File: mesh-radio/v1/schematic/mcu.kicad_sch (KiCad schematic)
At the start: 34 parts, among them U8 NRF52840-QIAA-F-R7, Y1 32MHz, Y2 32.768kHz

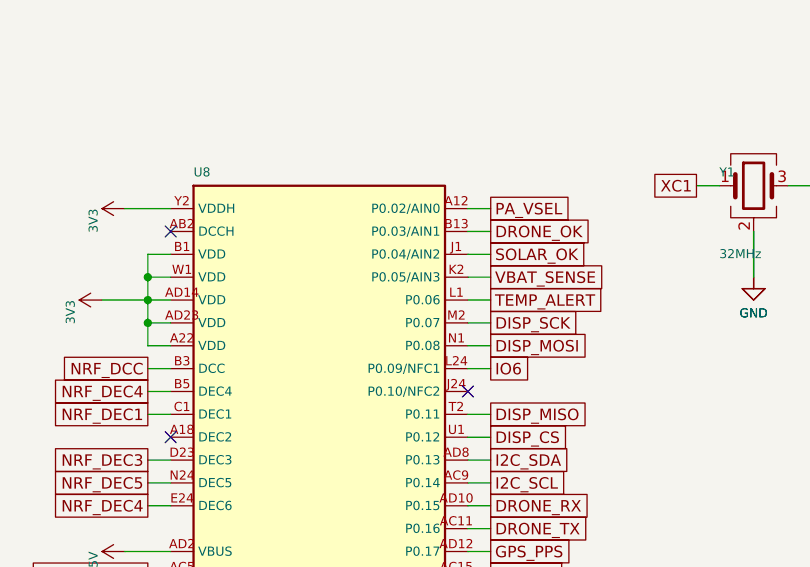
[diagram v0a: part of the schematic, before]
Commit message: Mesh Radio v1: fix every design-review finding, add the part audit
An independent review of the schematic found two critical and nine further
issues; all are fixed in src/circuit.py:
- reverse-battery FET gate now returns to the cell's own minus terminal, so
  a backwards cell stays isolated even while USB/solar/drone power the board
- solar and drone inputs: reverse-blocking Schottky + 22 V flat-clamp TVS
  (the 15 V TVS would have failed on a 12 V panel); 4.7 V clamp on every
  eFuse EN/UVLO pin so 20 V on an input stays inside its rating
- ideal diode (LM66100) holds VSYS on the cell when a 3 W burst trips the
  charger's 3.0 V battery disconnect
- charge LED moved to STAT2 (charging), USB cut-off lowered to 5.4 V,
  charger /CE on a GPIO for firmware temperature control, -40 C TCXO,
  power mux on only with the amplifier, header VSYS pin removed
- firmware ceilings documented: SX1262 +20 dBm, amplifier 3.6 V by default

docs/part-audit.md: all 125 lines checked at DigiKey and LCSC (genuine
LCSC numbers, DigiKey numbers, second sources for out-of-stock lines);
parts cost about $76 at 10 boards, $58 at 100.

Schematic regenerated: ERC 0 violations, netlist equals circuit.py.

Co-Authored-By: Claude Opus 5.5 <noreply@anthropic.com>
Claude-Session: https://claude.ai/code/session_015TBB2ThqxHSgA8MkFosmn9
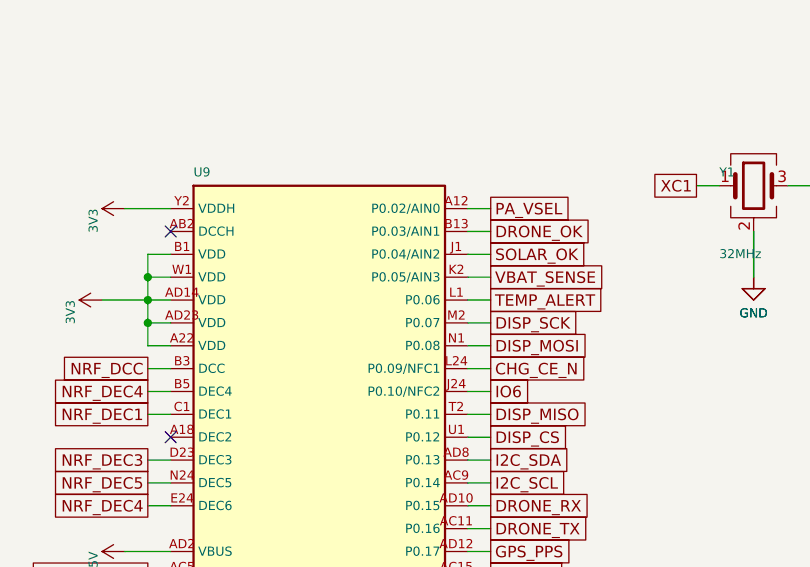
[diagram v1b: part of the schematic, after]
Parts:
- removed U8: NRF52840-QIAA-F-R7, og:AQFN-73_L7.0-W7.0-P0.50-BL-EP4.8, symbol og:NRF52840
- added U9: NRF52840-QIAA-F-R7, og:AQFN-73_L7.0-W7.0-P0.50-BL-EP4.8, symbol og:NRF52840
- AE1: DigiKey (none) -> 712-2450AT18A0100001ECT-ND
- C22, C27, C33, C34: DigiKey (none) -> 1276-1044-1-ND
- C23, C28: DigiKey (none) -> 1276-1067-1-ND
- C24, C25, C26, C30: DigiKey (none) -> 1276-1001-1-ND
- C29: DigiKey (none) -> 1276-1077-1-ND
- C31: DigiKey (none) -> 490-5922-1-ND
- C32: DigiKey (none) -> 490-3242-1-ND
- C35, C36: DigiKey (none) -> 1276-1178-1-ND
- C37, C38: DigiKey (none) -> 490-3113-1-ND
- C39: DigiKey (none) -> 490-6080-1-ND
- C40: DigiKey (none) -> 490-6077-1-ND
- C41: DigiKey (none) -> 490-6073-1-ND
- L2: DigiKey (none) -> 445-6396-1-ND
- L3: DigiKey (none) -> 490-1148-1-ND
- L4: DigiKey (none) -> 490-1139-1-ND
- L5: DigiKey (none) -> 490-6800-1-ND
- L6: DigiKey (none) -> 490-6813-1-ND
- R35, R36: DigiKey (none) -> 311-22.0LRCT-ND
- Y1: DigiKey (none) -> 535-13900-1-ND
- Y2: DigiKey (none) -> 535-9543-1-ND
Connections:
- net 3V3: now also U9.A22 (VDD), U9.AD14 (VDD), U9.AD23 (VDD), U9.B1 (VDD), U9.W1 (VDD), U9.Y2 (VDDH)
- net BTN_USER: now also U9.AD22 (P1.00)
- net CHG_STAT1: now also U9.AD20 (P0.24)
- net CHG_STAT2: now also U9.AC21 (P0.25)
- net DISP_BL: now also U9.P2 (P1.08)
- net DISP_CS: now also U9.U1 (P0.12)
- net DISP_DC: now also U9.G1 (P0.26)
- net DISP_MISO: now also U9.T2 (P0.11)
- net DISP_MOSI: now also U9.N1 (P0.08)
- net DISP_RST: now also U9.H2 (P0.27)
- net DISP_SCK: now also U9.M2 (P0.07)
- net DRONE_CTS: now also U9.AC17 (P0.21)
- net DRONE_OK: now also U9.B13 (P0.03/AIN1)
- net DRONE_RTS: now also U9.AD18 (P0.22)
- net DRONE_RX: now also U9.AD10 (P0.15)
- net DRONE_TX: now also U9.AC11 (P0.16)
- net GND: now also U9.0 (VSS (EP)), U9.B7 (VSS), U9.F23 (VSS_PA)
- net GPS_EN: now also U9.AC19 (P0.23)
- net GPS_PPS: now also U9.AD12 (P0.17)
- net GPS_RESET: now also U9.R1 (P1.09)
- net GPS_RX: now also U9.AC15 (P0.19)
- net GPS_TX: now also U9.AD16 (P0.20)
- net I2C_SCL: now also U9.AC9 (P0.14)
- net I2C_SDA: now also U9.AD8 (P0.13)
- net IO1: now also U9.B11 (P0.28/AIN4)
- net IO2: now also U9.A10 (P0.29/AIN5)
- net IO3: now also U9.B9 (P0.30/AIN6)
- net IO4: now also U9.A8 (P0.31/AIN7)
- net IO5: now also U9.W24 (P1.02)
- net IO6: now also U9.J24 (P0.10/NFC2)
- net LED_BLUE: now also U9.U24 (P1.04)
- net LED_GREEN: now also U9.V23 (P1.03)
- net LNA_EN: now also U9.T23 (P1.05)
- net LORA_BUSY: now also U9.B15 (P1.14)
- net LORA_DIO1: now also U9.A14 (P1.15)
- net LORA_MISO: now also U9.A16 (P1.13)
- net LORA_MOSI: now also U9.B17 (P1.12)
- net LORA_NRESET: now also U9.R24 (P1.06)
- net LORA_NSS: now also U9.A20 (P1.10)
- net LORA_SCK: now also U9.B19 (P1.11)
- net NRF_ANT: now also U9.H23 (ANT)
- net NRF_DCC: now also U9.B3 (DCC)
- net NRF_DEC1: now also U9.C1 (DEC1)
- net NRF_DEC3: now also U9.D23 (DEC3)
- net NRF_DEC4: now also U9.B5 (DEC4), U9.E24 (DEC6)
- net NRF_DEC5: now also U9.N24 (DEC5)
- net NRF_DECUSB: now also U9.AC5 (DECUSB)
- net NRF_DM: now also U9.AD4 (D-)
- net NRF_DP: now also U9.AD6 (D+)
- net NRF_RESET: now also U9.AC13 (P0.18/nRESET)
- net PA_EN: now also U9.P23 (P1.07)
- net PA_PWR_EN: now also U9.Y23 (P1.01)
- net PA_VSEL: now also U9.A12 (P0.02/AIN0)
- net SOLAR_OK: now also U9.J1 (P0.04/AIN2)
- net SWDCLK: now also U9.AA24 (SWDCLK)
- net SWDIO: now also U9.AC24 (SWDIO)
- net TEMP_ALERT: now also U9.L1 (P0.06)
- net USB_5V: now also U9.AD2 (VBUS)
- net VBAT_SENSE: now also U9.K2 (P0.05/AIN3)
- net XC1: now also U9.B24 (XC1)
- net XC2: now also U9.A23 (XC2)
- net XL1: now also U9.D2 (P0.00/XL1)
- net XL2: now also U9.F2 (P0.01/XL2)
- new net CHG_CE_N: U9.L24 (P0.09/NFC1)
- no-connect marks 4 -> 3

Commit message: Mesh radio v1: RF fixes from sim/rf (3 W heating, pad power, filter loss)
sim/rf found three failures at 3 W; fixed with the same part count:
- the amplifier output-match inductor and the two harmonic-filter
  inductors ran 1.1-2.7x past their rated self-heating: now Murata
  LQW2BAN 0805 wire-wound (2 A class), 3.6 / 3.2 / 3.2 nH;
- the harmonic filter's values move (2.0, 3.2 nH || 3.6 pF, 1.3,
  3.2 nH || 1.3 pF, 0.9 pF, Murata GQM1875 250 V C0G): 0.3 dB less loss,
  so 3 W reaches the U.FL; 2f-5f harmonic yield stays 100 % at
  -40..85 C;
- the pad's first 68 R reached 114 % of its rating at +22 dBm drive and
  85 C: now Vishay RCS0805 anti-surge, 0.4 W;
- the Bluetooth match's 0.8 pF is the +-0.05 pF grade (100 % yield).
Schematic regenerated: ERC 0, netlist equals circuit.py.  sim/rf
snapshot included; the open-antenna and 6f-10f checks are still running.

Co-Authored-By: Claude Opus 5.5 <noreply@anthropic.com>
Claude-Session: https://claude.ai/code/session_015TBB2ThqxHSgA8MkFosmn9
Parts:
- C39: DigiKey 490-6080-1-ND -> (none); LCSC C76915 -> C88902; MPN GJM1555C1HR80BB01D -> GJM1555C1HR80WB01D
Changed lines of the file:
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@@
 			)
 		)
-		(property "MPN" "GJM1555C1HR80BB01D"
+		(property "MPN" "GJM1555C1HR80WB01D"
 			(at 241.3 203.2 0)
 			(effects
@@
 			)
 		)
-		(property "DigiKey" "490-6080-1-ND"
+		(property "LCSC" "C88902"
 			(at 241.3 203.2 0)
 			(effects
@@
 			)
 		)
-		(property "LCSC" "C76915"
+		(property "Description" "Capacitor 0.8pF 50V C0G high-Q +-0.05pF 0402"
 			(at 241.3 203.2 0)
 			(effects
-				(font
-					(size 1.27 1.27)
-				)
-				(hide yes)
-			)
-		)
-		(property "Description" "Capacitor 0.8pF 50V C0G high-Q 0402"
-			(at 241.3 203.2 0)
-			(effects

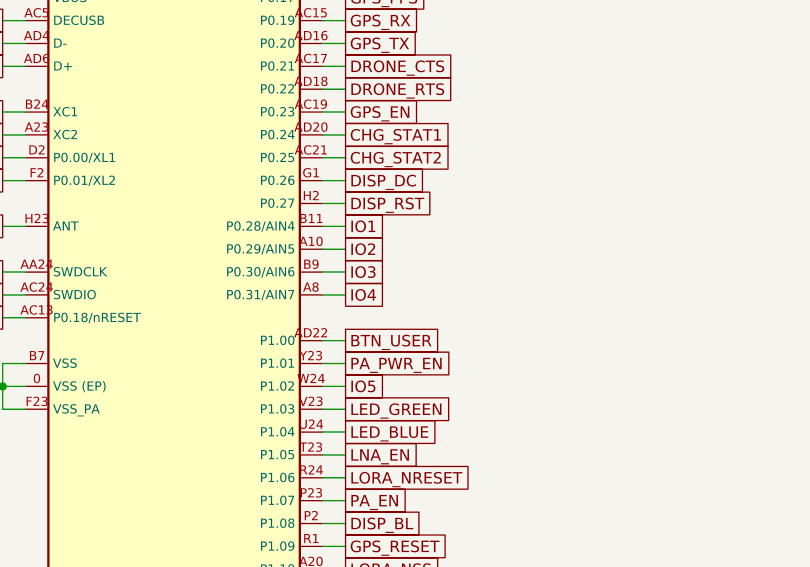
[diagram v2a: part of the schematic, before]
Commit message: Mesh radio v1: LFCG-1000+ antenna filter; missing-antenna detector
Owner decisions of 19 Oct: keep 3 W with the heat fixes and a gap pad to
a metal enclosure, 6 layers, 300 mA charging, new parts at the designer's
judgement.  This commit, from sim/rf:
- FL1 LFCN-1000+ (1206) -> LFCG-1000+ (0805, 8 pads, Mini-Circuits case
  GE0805C-2: in 8, out 4): no stop-band re-entry at 5.5-10 GHz, where the
  3 W 6th-10th harmonics failed FCC's restricted-band limit;
- a reflected-wave detector: a printed line beside the ANT line
  terminated in 49.9 R, an Infineon BAT15-02EL, 1 nF and 100 k into
  P0.30/AIN6, so firmware can cut the amplifier within ~1 ms of a packet
  with no antenna (the antenna switch sees 109-160 % of its rating then);
- P0.31/AIN7 reads the charger's NTC (firmware's 0-45 C charging rule);
  the expansion header's IO3/IO4 give way (four spare pins remain).
ERC 0, netlist equals circuit.py, every pin and pad accounted for.

Co-Authored-By: Claude Opus 5.5 <noreply@anthropic.com>
Claude-Session: https://claude.ai/code/session_015TBB2ThqxHSgA8MkFosmn9
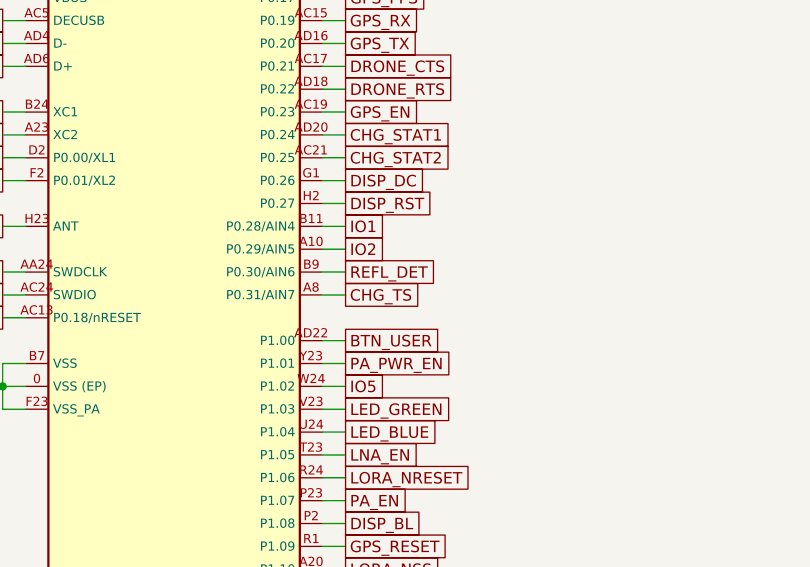
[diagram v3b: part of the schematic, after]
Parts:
- C39: DigiKey (none) -> 490-11253-1-ND
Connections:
- net IO3 renamed REFL_DET
- net IO4 renamed CHG_TS
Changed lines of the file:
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@@
 		)
 	)
-	(global_label "IO3"
+	(global_label "REFL_DET"
 		(shape passive)
 		(at 74.93 116.84 0)
@@
 		)
 	)
-	(global_label "IO4"
+	(global_label "CHG_TS"
 		(shape passive)
 		(at 74.93 119.38 0)
@@
 			(at 241.3 203.2 0)
 			(effects
+				(font
+					(size 1.27 1.27)
+				)
+				(hide yes)
+			)
+		)
+		(property "DigiKey" "490-11253-1-ND"
+			(at 241.3 203.2 0)
+			(effects

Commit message: Mesh radio v1: power-path and firmware rework in progress (snapshot)
Co-Authored-By: Claude Opus 5.5 <noreply@anthropic.com>
Claude-Session: https://claude.ai/code/session_015TBB2ThqxHSgA8MkFosmn9
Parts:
- removed C40: 0.5pF, og:C_0402, symbol Device:C
- removed C41: 1.0pF, og:C_0402, symbol Device:C
- removed R35, R36: 22R, og:R_0402, symbol Device:R
- removed U9: NRF52840-QIAA-F-R7, og:AQFN-73_L7.0-W7.0-P0.50-BL-EP4.8, symbol og:NRF52840
- added C20: 4.7uF, og:C_0603, symbol Device:C
- added C21: 1uF, og:C_0402, symbol Device:C
- added R40, R41: 22R, og:R_0402, symbol Device:R
- added U8: NRF52840-QIAA-F-R7, og:AQFN-73_L7.0-W7.0-P0.50-BL-EP4.8, symbol og:NRF52840
- C22: value 4.7uF -> 100nF; footprint og:C_0603 -> og:C_0402; DigiKey 1276-1044-1-ND -> 1276-1001-1-ND; LCSC C1705 -> C1525; MPN CL10A475KP8NNNC -> CL05B104KO5NNNC
- C23, C28: value 1uF -> 100nF; DigiKey 1276-1067-1-ND -> 1276-1001-1-ND; LCSC C29266 -> C1525; MPN CL05A105KO5NNNC -> CL05B104KO5NNNC
- C25: value 100nF -> 4.7uF; footprint og:C_0402 -> og:C_0603; DigiKey 1276-1001-1-ND -> 1276-1044-1-ND; LCSC C1525 -> C1705; MPN CL05B104KO5NNNC -> CL10A475KP8NNNC
- C26: value 100nF -> 1uF; DigiKey 1276-1001-1-ND -> 1276-1067-1-ND; LCSC C1525 -> C29266; MPN CL05B104KO5NNNC -> CL05A105KO5NNNC
- C27: value 4.7uF -> 47nF; footprint og:C_0603 -> og:C_0402; DigiKey 1276-1044-1-ND -> 1276-1077-1-ND; LCSC C1705 -> C307434; MPN CL10A475KP8NNNC -> CL05B473KO5NNNC
- C29: value 47nF -> 100pF; DigiKey 1276-1077-1-ND -> 490-5922-1-ND; LCSC C307434 -> C77177; MPN CL05B473KO5NNNC -> GRM1555C1H101JA01D; Manufacturer Samsung Electro-Mechanics -> Murata
- C30: value 100nF -> 820pF; DigiKey 1276-1001-1-ND -> 490-3242-1-ND; LCSC C1525 -> C85943; MPN CL05B104KO5NNNC -> GRM1555C1H821JA01D; Manufacturer Samsung Electro-Mechanics -> Murata
- C31: value 100pF -> 4.7uF; footprint og:C_0402 -> og:C_0603; DigiKey 490-5922-1-ND -> 1276-1044-1-ND; LCSC C77177 -> C1705; MPN GRM1555C1H101JA01D -> CL10A475KP8NNNC; Manufacturer Murata -> Samsung Electro-Mechanics
- C32: value 820pF -> 4.7uF; footprint og:C_0402 -> og:C_0603; DigiKey 490-3242-1-ND -> 1276-1044-1-ND; LCSC C85943 -> C1705; MPN GRM1555C1H821JA01D -> CL10A475KP8NNNC; Manufacturer Murata -> Samsung Electro-Mechanics
- C33, C34: value 4.7uF -> 12pF; footprint og:C_0603 -> og:C_0402; DigiKey 1276-1044-1-ND -> 1276-1178-1-ND; LCSC C1705 -> C26406; MPN CL10A475KP8NNNC -> CL05C120JB5NNNC
- C35, C36: value 12pF -> 10pF; DigiKey 1276-1178-1-ND -> 490-3113-1-ND; LCSC C26406 -> C85874; MPN CL05C120JB5NNNC -> GJM1555C1H100JB01D; Manufacturer Samsung Electro-Mechanics -> Murata
- C37: value 10pF -> 0.8pF; DigiKey 490-3113-1-ND -> 490-11253-1-ND; LCSC C85874 -> C88902; MPN GJM1555C1H100JB01D -> GJM1555C1HR80WB01D
- C38: value 10pF -> 0.5pF; DigiKey 490-3113-1-ND -> 490-6077-1-ND; LCSC C85874 -> C76911; MPN GJM1555C1H100JB01D -> GJM1555C1HR50BB01D
- C39: value 0.8pF -> 1.0pF; DigiKey 490-11253-1-ND -> 490-6073-1-ND; LCSC C88902 -> C76898; MPN GJM1555C1HR80WB01D -> GJM1555C1H1R0BB01D
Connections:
- net USB_5V is gone; now on net XC1: C33.1
- net 3V3: now also C20.1, C21.1, U8.A22 (VDD), U8.AD14 (VDD), U8.AD23 (VDD), U8.B1 (VDD), U8.W1 (VDD), U8.Y2 (VDDH); no longer C26.1, C27.1
- net BLE_50R: now also C38.1, C39.1
- net BLE_T: now also C39.2
- net BTN_USER: now also U8.AD22 (P1.00)
- net CHG_CE_N: now also U8.L24 (P0.09/NFC1)
- net CHG_STAT1: now also U8.AD20 (P0.24)
- net CHG_STAT2: now also U8.AC21 (P0.25)
- net CHG_TS: now also U8.A8 (P0.31/AIN7)
- net DISP_BL: now also U8.P2 (P1.08)
- net DISP_CS: now also U8.U1 (P0.12)
- net DISP_DC: now also U8.G1 (P0.26)
- net DISP_MISO: now also U8.T2 (P0.11)
- net DISP_MOSI: now also U8.N1 (P0.08)
- net DISP_RST: now also U8.H2 (P0.27)
- net DISP_SCK: now also U8.M2 (P0.07)
- net DRONE_CTS: now also U8.AC17 (P0.21)
- net DRONE_OK: now also U8.B13 (P0.03/AIN1)
- net DRONE_RTS: now also U8.AD18 (P0.22)
- net DRONE_RX: now also U8.AD10 (P0.15)
- net DRONE_TX: now also U8.AC11 (P0.16)
- net GND: now also C20.2, C21.2, U8.0 (VSS (EP)), U8.B7 (VSS), U8.F23 (VSS_PA); no longer C39.2
- net GPS_EN: now also U8.AC19 (P0.23)
- net GPS_PPS: now also U8.AD12 (P0.17)
- net GPS_RESET: now also U8.R1 (P1.09)
- net GPS_RX: now also U8.AC15 (P0.19)
- net GPS_TX: now also U8.AD16 (P0.20)
- net I2C_SCL: now also U8.AC9 (P0.14)
- net I2C_SDA: now also U8.AD8 (P0.13)
- net IO1: now also U8.B11 (P0.28/AIN4)
- net IO2: now also U8.A10 (P0.29/AIN5)
- net IO5: now also U8.W24 (P1.02)
- net IO6: now also U8.J24 (P0.10/NFC2)
- net LED_BLUE: now also U8.U24 (P1.04)
- net LED_GREEN: now also U8.V23 (P1.03)
- net LNA_EN: now also U8.T23 (P1.05)
- net LORA_BUSY: now also U8.B15 (P1.14)
- net LORA_DIO1: now also U8.A14 (P1.15)
- net LORA_MISO: now also U8.A16 (P1.13)
- net LORA_MOSI: now also U8.B17 (P1.12)
- net LORA_NRESET: now also U8.R24 (P1.06)
- net LORA_NSS: now also U8.A20 (P1.10)
- net LORA_SCK: now also U8.B19 (P1.11)
- net NRF_ANT: now also C37.1, U8.H23 (ANT); no longer C39.1
- net NRF_DCC: now also U8.B3 (DCC)
- net NRF_DEC1: now also C28.1, U8.C1 (DEC1); no longer C30.1
- net NRF_DEC3: now also C29.1, U8.D23 (DEC3); no longer C31.1
- net NRF_DEC4: now also C26.1, C27.1, U8.B5 (DEC4), U8.E24 (DEC6); no longer C28.1, C29.1
- net NRF_DEC5: now also C30.1, U8.N24 (DEC5); no longer C32.1
- net NRF_DECUSB: now also C32.1, U8.AC5 (DECUSB); no longer C34.1
- net NRF_DM: now also R41.2, U8.AD4 (D-)
- net NRF_DP: now also R40.2, U8.AD6 (D+)
- net NRF_RESET: now also U8.AC13 (P0.18/nRESET)
- net PA_EN: now also U8.P23 (P1.07)
- net PA_PWR_EN: now also U8.Y23 (P1.01)
- net REFL_DET: now also U8.B9 (P0.30/AIN6)
- net SOLAR_OK: now also U8.J1 (P0.04/AIN2)
- net SWDCLK: now also U8.AA24 (SWDCLK)
- net SWDIO: now also U8.AC24 (SWDIO)
- net TEMP_ALERT: now also U8.L1 (P0.06)
- net USB_DM: now also R41.1
- net USB_DP: now also R40.1
- net VBAT_SENSE: now also U8.K2 (P0.05/AIN3)
- net XC1: now also U8.B24 (XC1); no longer C35.1
- net XC2: now also C34.1, U8.A23 (XC2); no longer C36.1
- net XL1: now also C35.1, U8.D2 (P0.00/XL1); no longer C37.1
- net XL2: now also C36.1, U8.F2 (P0.01/XL2); no longer C38.1
- new net NRF_VBUS: C31.1, U8.AD2 (VBUS)
- new net PA_SRC_SYS: U8.A12 (P0.02/AIN0)
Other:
- moved on the sheet: C22, C23, C24, C25, C26, C27, C28, C29, C30, C31, C32, C33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
